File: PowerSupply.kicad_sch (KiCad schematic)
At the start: 4 parts, among them U2 TPS62177DQC

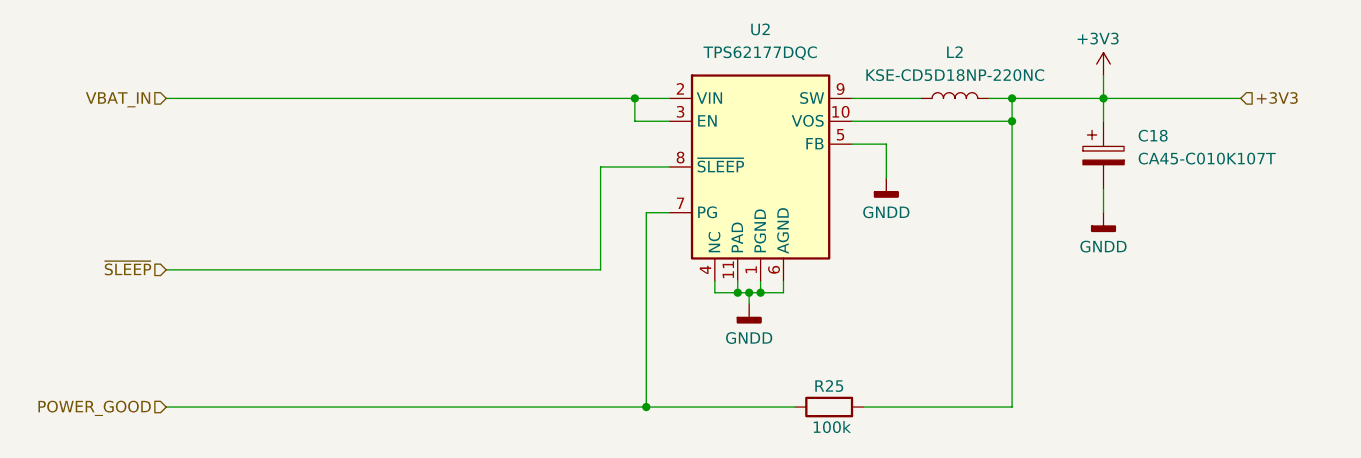
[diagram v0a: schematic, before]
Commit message: Dual SIM version
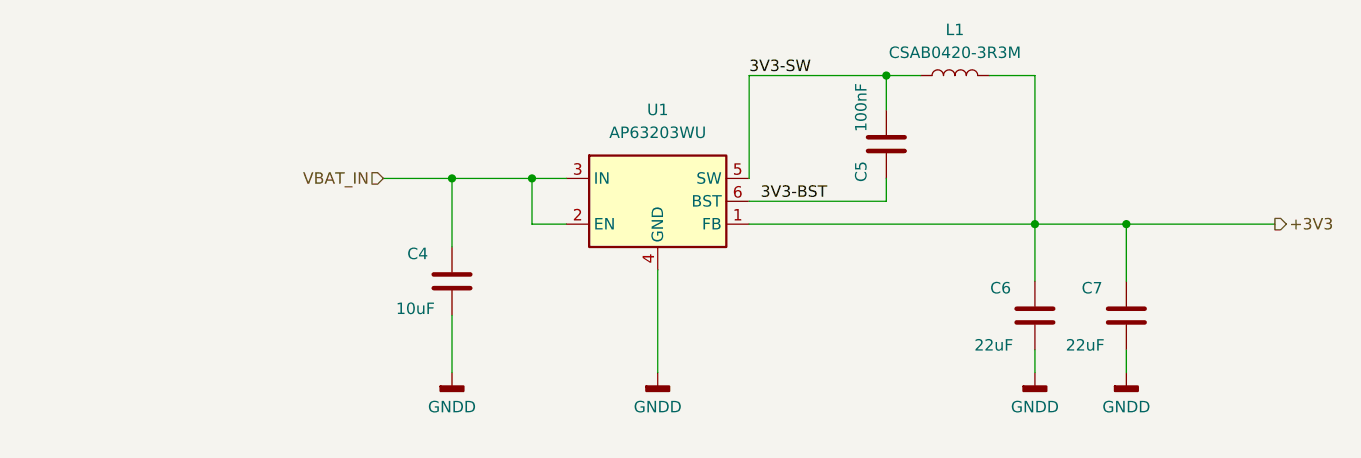
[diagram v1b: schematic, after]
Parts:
- removed C18: CA45-C010K107T, Capacitor_Tantalum_SMD:CP_EIA-6032-28_Kemet-C_Pad2.25x2.35mm_HandSolder, symbol Device:C_Polarized
- removed L2: KSE-CD5D18NP-220NC, Inductor_SMD:L_Cenker_CKCS6028, symbol Device:L
- removed R25: 100k, Resistor_SMD:R_0805_2012Metric_Pad1.20x1.40mm_HandSolder, symbol Device:R
- removed U2: TPS62177DQC, Package_SON:WSON-10-1EP_2x3mm_P0.5mm_EP0.84x2.4mm_ThermalVias, symbol Regulator_Switching:TPS62177DQC
- added C4: 10uF, Capacitor_SMD:C_0805_2012Metric_Pad1.18x1.45mm_HandSolder, symbol Device:C
- added C5: 100nF, Capacitor_SMD:C_0805_2012Metric_Pad1.18x1.45mm_HandSolder, symbol Device:C
- added C6, C7: 22uF, Capacitor_SMD:C_0805_2012Metric_Pad1.18x1.45mm_HandSolder, symbol Device:C
- added L1: CSAB0420-3R3M, footprints:CSAB0420-4.4x4.4mm, symbol Device:L
- added U1: AP63203WU, Package_TO_SOT_SMD:TSOT-23-6, symbol Regulator_Switching:AP63203WU
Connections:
- net +3V3: now also C6.2, C7.2, L1.2, U1.1 (FB)
- net GNDD: now also C4.1, C6.1, C7.1, U1.4 (GND)
- net VBAT_IN: now also C4.2, U1.2 (EN), U1.3 (IN)
- new net 3V3-BST: C5.1, U1.6 (BST)
- new net 3V3-SW: C5.2, L1.1, U1.5 (SW)
